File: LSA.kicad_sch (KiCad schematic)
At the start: 4 parts, among them J1 685119248123, J2 685119248123

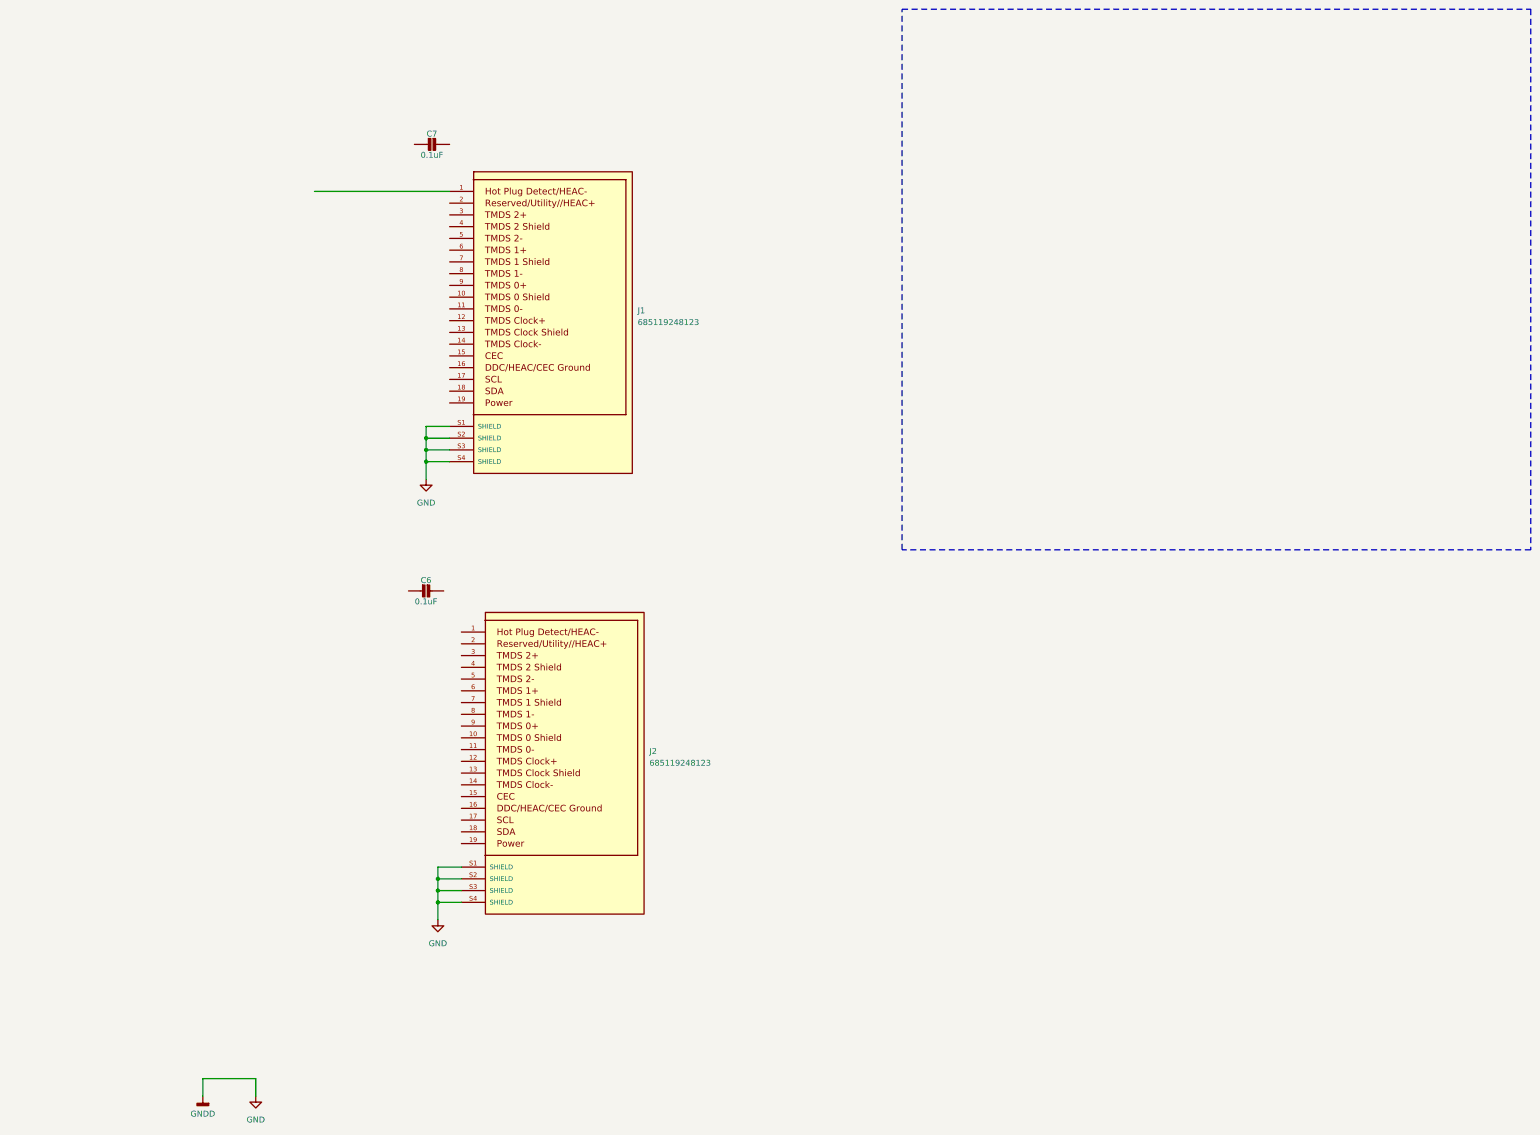
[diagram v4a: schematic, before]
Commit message: Electrical Rules Check fixes in progress.
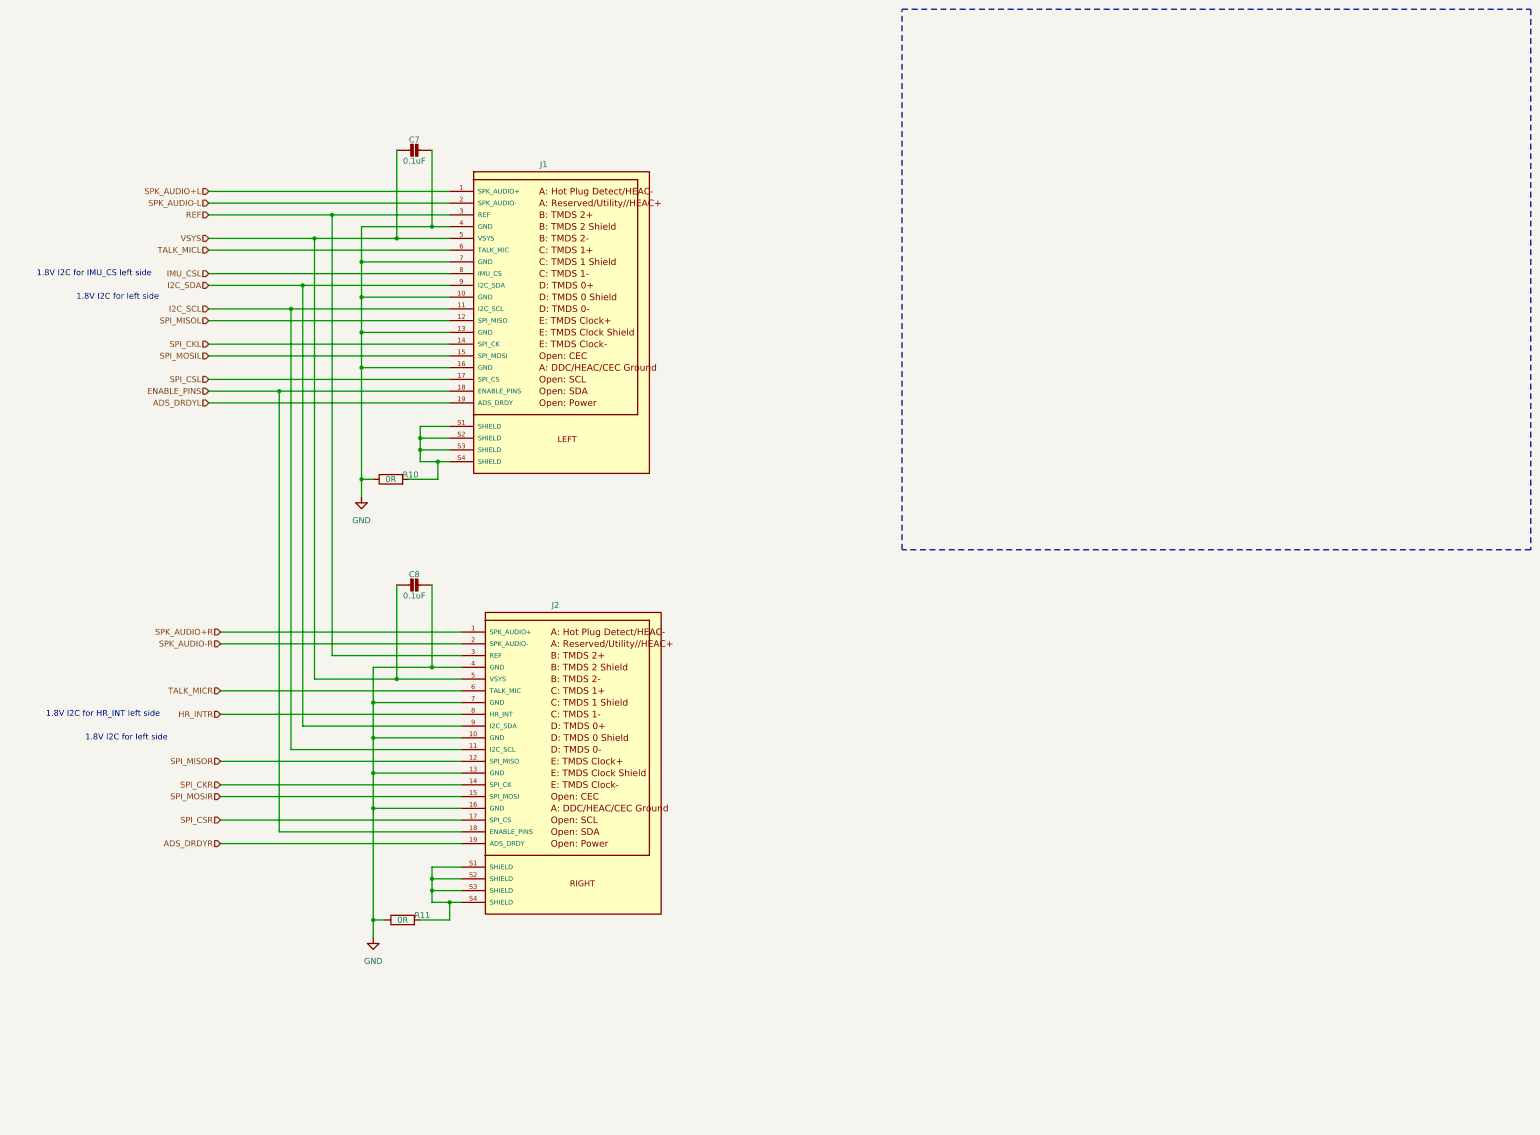
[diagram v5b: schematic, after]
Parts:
- removed C6: 0.1uF, Mustang_Library:C_0805_2012Metric_Pad1.18x1.45mm_HandSolder, symbol Mustang_Library:CAP_CERAMIC0805-NOOUTLINE
- added C8: 0.1uF, Mustang_Library:C_0805_2012Metric_Pad1.18x1.45mm_HandSolder, symbol Mustang_Library:CAP_CERAMIC0805-NOOUTLINE
- added R10, R11: 0R, symbol Mustang_Library:R_h
- J1: symbol Mustang_Library:685119248123 -> Mustang_Library:685119248123_Left; Side (none) -> LEFT
- J2: symbol Mustang_Library:685119248123 -> Mustang_Library:685119248123_Right; Side (none) -> RIGHT
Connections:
- net GND: now also C7.1, J1.10 (GND), J1.13 (GND), J1.16 (GND), J1.4 (GND), J1.7 (GND), J2.10 (GND), J2.13 (GND), J2.16 (GND), J2.4 (GND), J2.7 (GND), C8.1, R10.1, R11.1; no longer J1.S1 (SHIELD), J1.S2 (SHIELD), J1.S3 (SHIELD), J1.S4 (SHIELD), J2.S1 (SHIELD), J2.S2 (SHIELD), J2.S3 (SHIELD), J2.S4 (SHIELD)
- net SPK_AUDIO+L: now reaches J1.1 (SPK_AUDIO+)
- net I2C_SCL: now reaches J1.11 (I2C_SCL)
- net I2C_SCL: now also J2.11 (I2C_SCL)
- net SPI_MISOL: now reaches J1.12 (SPI_MISO)
- net SPI_CKL: now reaches J1.14 (SPI_CK)
- net SPI_MOSIL: now reaches J1.15 (SPI_MOSI)
- net SPI_CSL: now reaches J1.17 (SPI_CS)
- net ENABLE_PINS: now reaches J1.18 (ENABLE_PINS)
- net ENABLE_PINS: now also J2.18 (ENABLE_PINS)
- net ADS_DRDYL: now reaches J1.19 (ADS_DRDY)
- net SPK_AUDIO-L: now reaches J1.2 (SPK_AUDIO-)
- net REF: now reaches J1.3 (REF)
- net REF: now also J2.3 (REF)
- net VSYS: now reaches J1.5 (VSYS)
- net VSYS: now also C7.2, J2.5 (VSYS), C8.2
- net TALK_MICL: now reaches J1.6 (TALK_MIC)
- net IMU_CSL: now reaches J1.8 (IMU_CS)
- net I2C_SDA: now reaches J1.9 (I2C_SDA)
- net I2C_SDA: now also J2.9 (I2C_SDA)
- net SPK_AUDIO+R: now reaches J2.1 (SPK_AUDIO+)
- net SPI_MISOR: now reaches J2.12 (SPI_MISO)
- net SPI_CKR: now reaches J2.14 (SPI_CK)
- net SPI_MOSIR: now reaches J2.15 (SPI_MOSI)
- net SPI_CSR: now reaches J2.17 (SPI_CS)
- net ADS_DRDYR: now reaches J2.19 (ADS_DRDY)
- net SPK_AUDIO-R: now reaches J2.2 (SPK_AUDIO-)
- net TALK_MICR: now reaches J2.6 (TALK_MIC)
- net HR_INTR: now reaches J2.8 (HR_INT)
- new net: J1.S1 (SHIELD), J1.S2 (SHIELD), J1.S3 (SHIELD), J1.S4 (SHIELD), R10.2
- new net: J2.S1 (SHIELD), J2.S2 (SHIELD), J2.S3 (SHIELD), J2.S4 (SHIELD), R11.2
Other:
- note added: "1.8V I2C for HR_INT left side"
- note added: "1.8V I2C for IMU_CS left side"
- note added: "1.8V I2C for left side"
- moved on the sheet: C7

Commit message: Use all YAGEO 0603 resistors.
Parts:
- R10, R11: footprint (none) -> Mustang_Library:R_0603_1608Metric; symbol Mustang_Library:R_h -> Mustang_Library:R_0603_0R; MPN (none) -> AC0603JR-070RL; Manufacturer (none) -> Yageo; Power (none) -> J
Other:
- moved on the sheet: J1
